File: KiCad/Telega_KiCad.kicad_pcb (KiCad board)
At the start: 2 copper layers, 180 x 140 mm, 70 parts, among them J501 Conn_24V, J502 Conn_12V, J503 Conn_Extra_5V, J504 Conn_Extra_15V, J505 Conn_Extra_Gnd1, J506 Conn_Extra_Gnd2, J601 USB_B, J602 Control_connector, SW501 SW_24V, SW502 SW_12V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

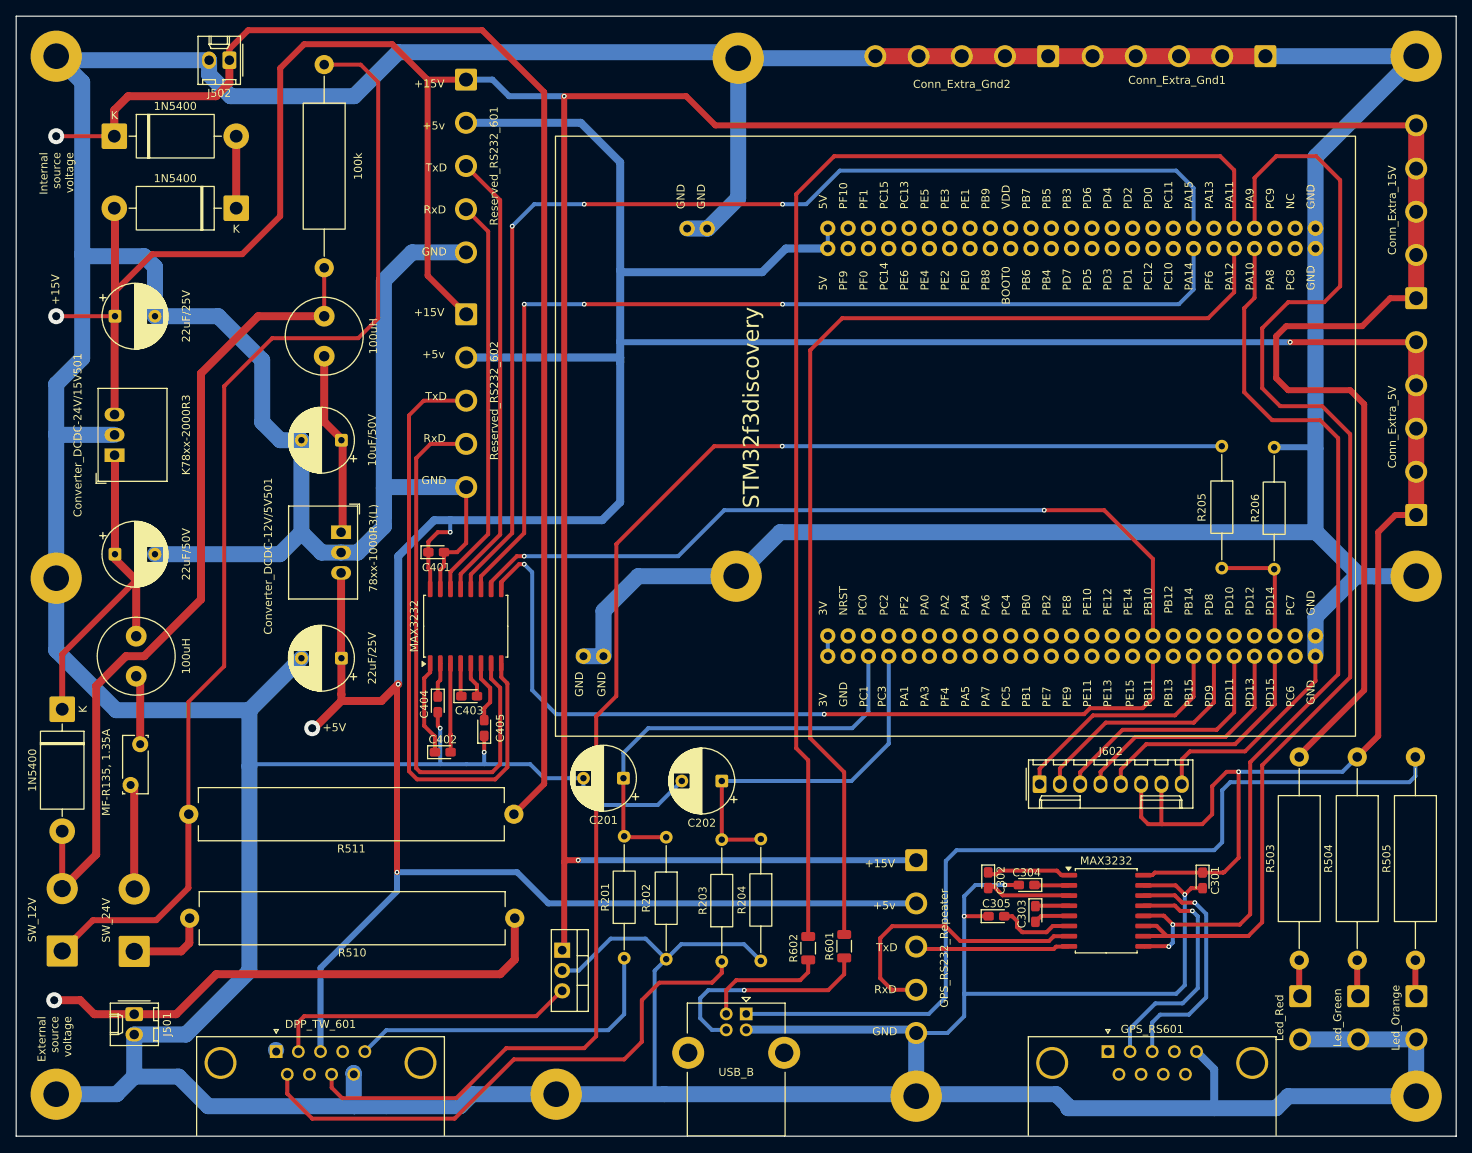
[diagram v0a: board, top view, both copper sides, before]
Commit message: Выровнял посадочные места на плате
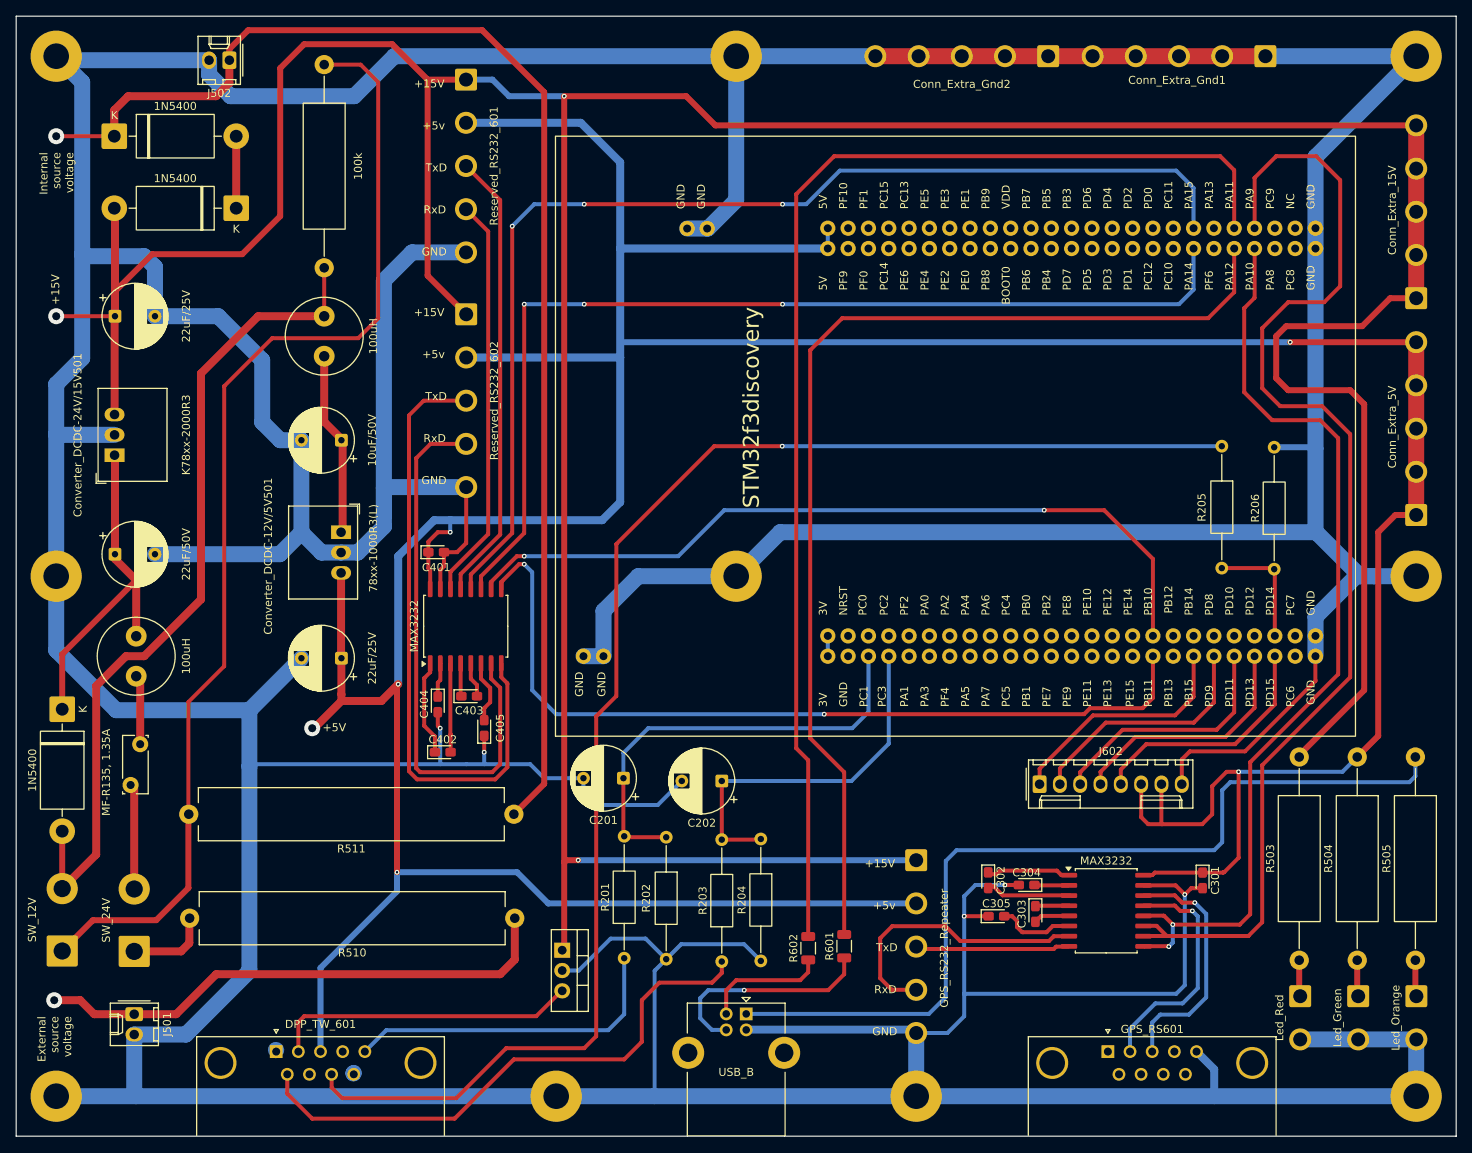
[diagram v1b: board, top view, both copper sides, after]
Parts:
- moved REF** 0.35 mm to (140.0, 55.0)
- moved REF** 0.25 mm to (55.0, 185.0)
- moved REF** 0.25 mm to (55.0, 120.0)
- moved REF** 0.25 mm to (117.5, 185.0)
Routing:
- net GND: track 1199.5 -> 1192.6 mm
- net +5V: track 538.0 -> 536.0 mm
